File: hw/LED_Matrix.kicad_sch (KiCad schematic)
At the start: 0 parts

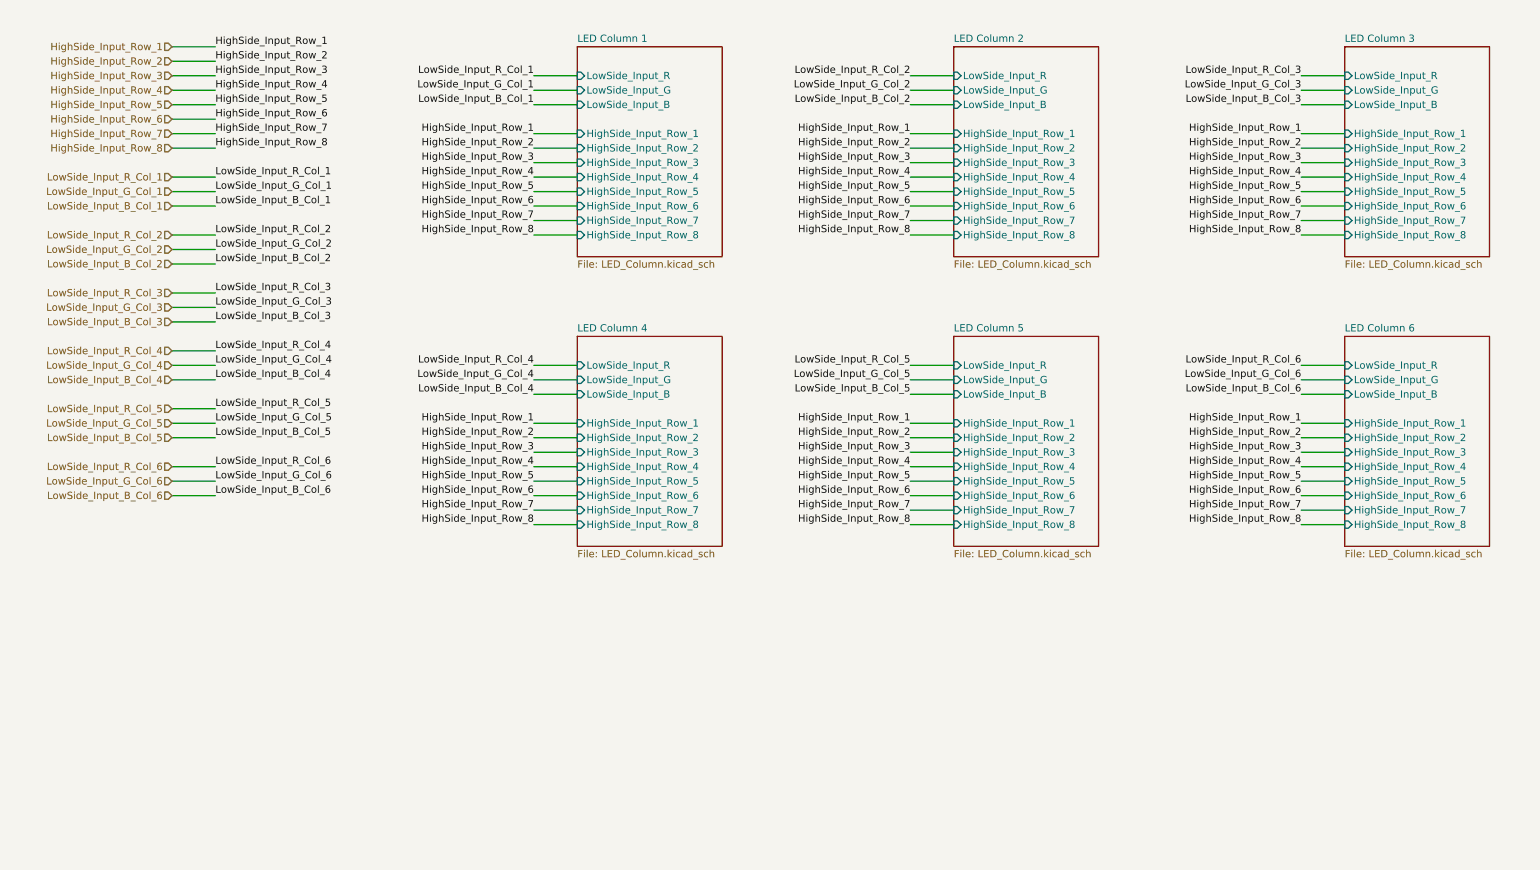
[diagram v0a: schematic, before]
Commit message: added NMOS matrix
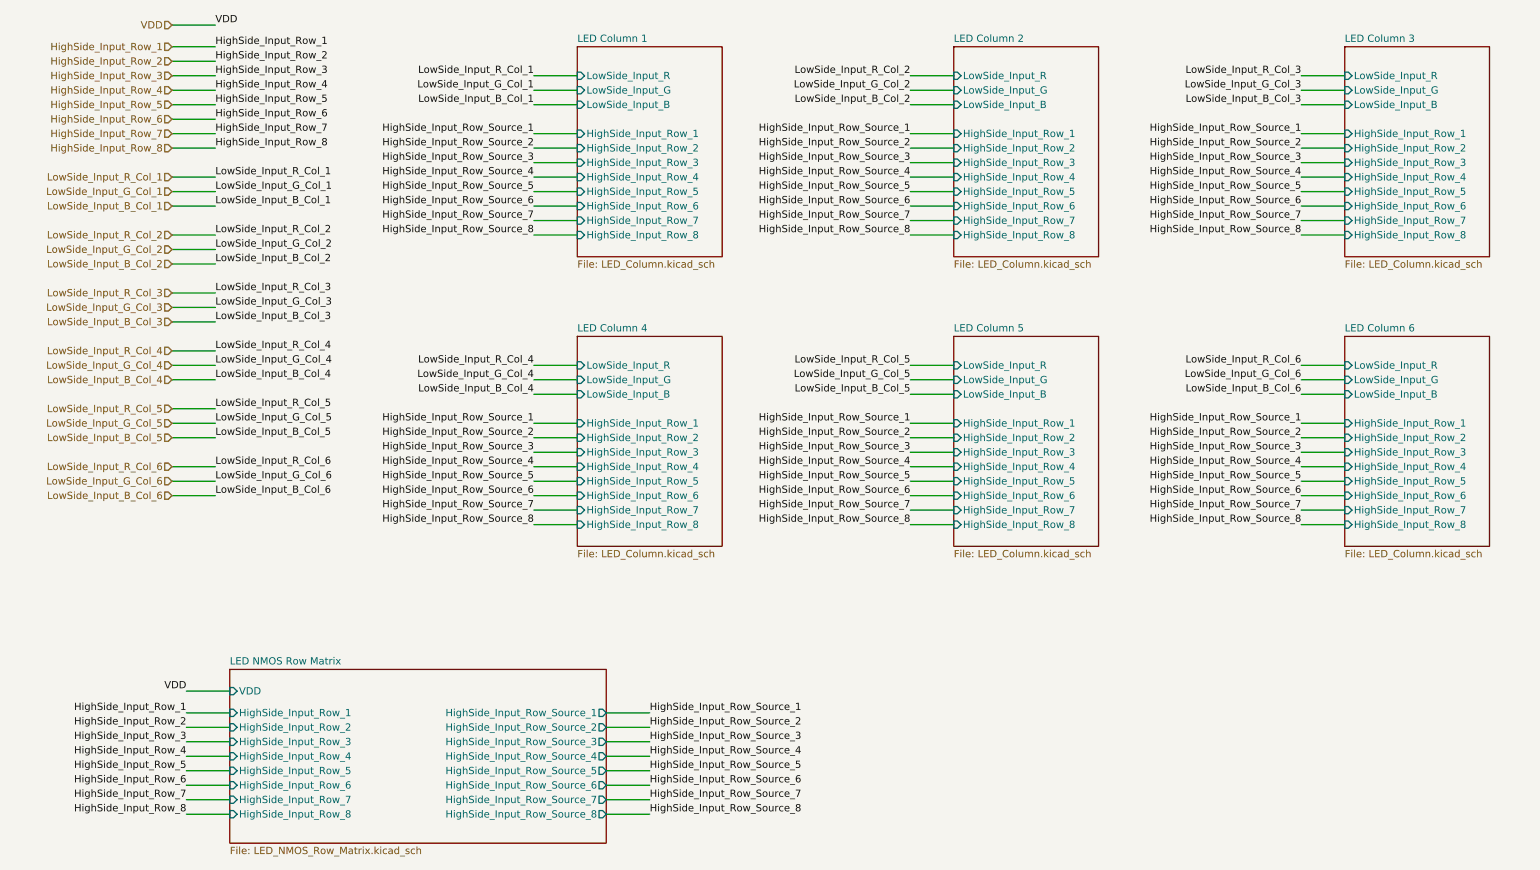
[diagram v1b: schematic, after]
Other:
- added sheet LED NMOS Row Matrix (LED_NMOS_Row_Matrix.kicad_sch)

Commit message: updated sheets information
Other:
- company: (none) -> Qingdao IotPi Information Technology Ltd.,
- title: (none) -> KiCad 2023 Shen Zhen Badge
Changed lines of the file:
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@@
 (kicad_sch (version 20230121) (generator eeschema)
   (paper "A4")
+  (title_block
+    (title "KiCad 2023 Shen Zhen Badge")
+    (date "2023-09-04")
+    (rev "1")
+    (company "Qingdao IotPi Information Technology Ltd.,")
+    (comment 1 "Designed by Yang Hongbo")
+  )
   (wire (pts (xy 53.34 133.35) (xy 45.72 133.35))
     (stroke (width 0) (type default))
